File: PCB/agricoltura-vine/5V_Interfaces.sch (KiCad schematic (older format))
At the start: 9 parts, among them K1 G5LE-14_DC5, K2 G5LE-14_DC5, T19 TSW-108-07-G-T, T22 0395121006, U8 TCA6416ARTWR

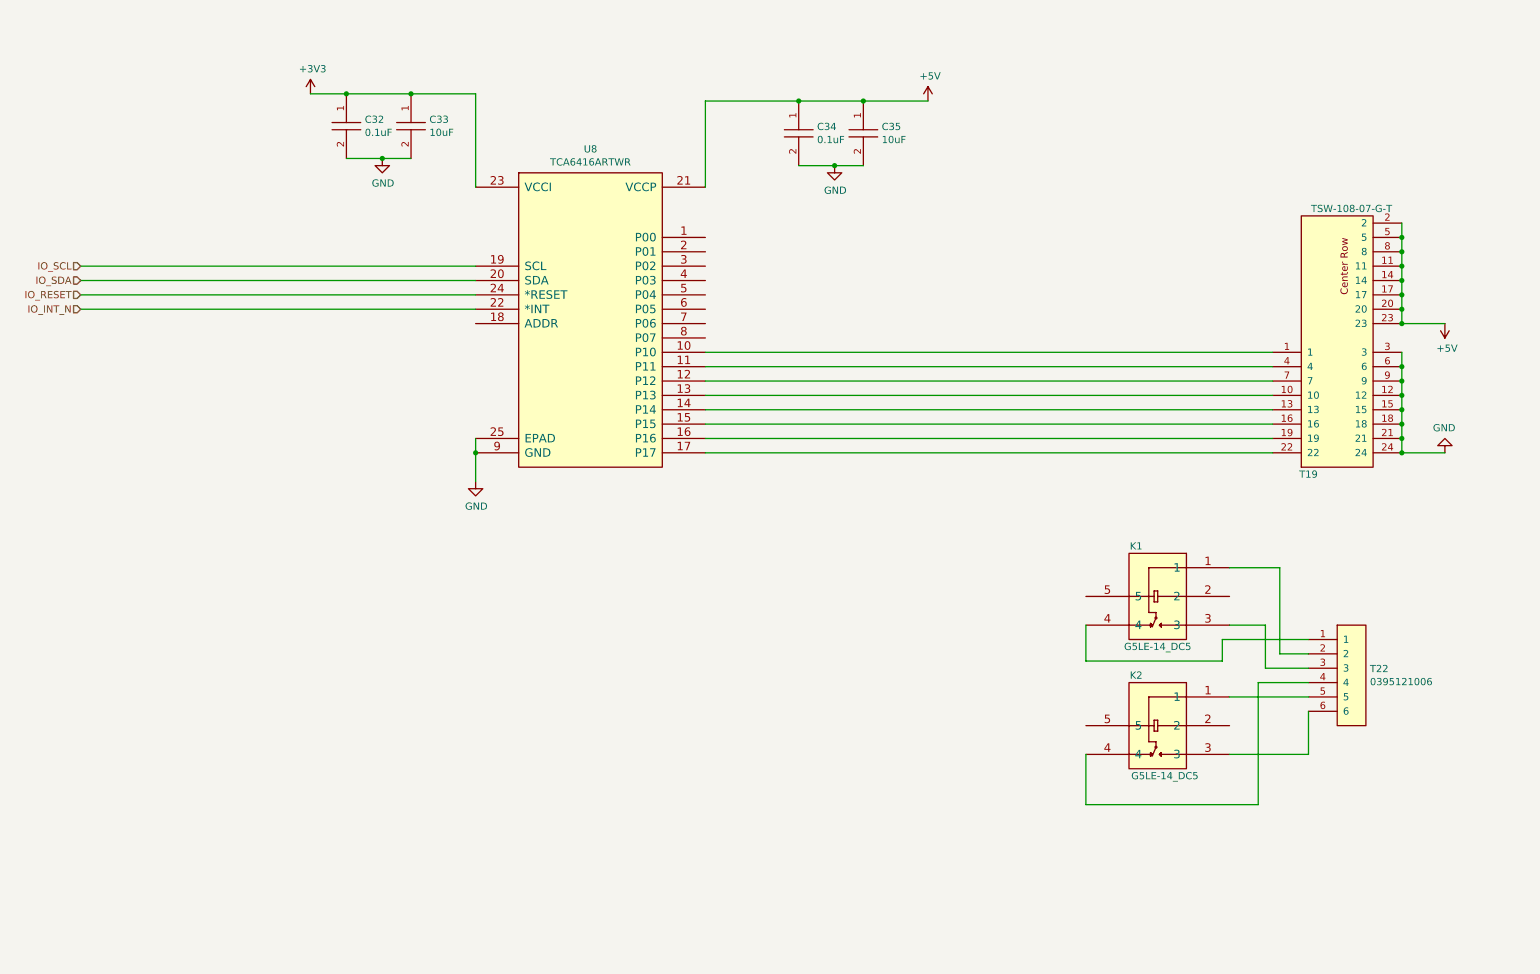
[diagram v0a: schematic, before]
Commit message: Relay Driver Circuit, Board Size Change
Added the Relay driver circuitry, increased size of board tobetter acccomodate relays, figuredout the powerplane topology to get 5Vs where it needs to go.
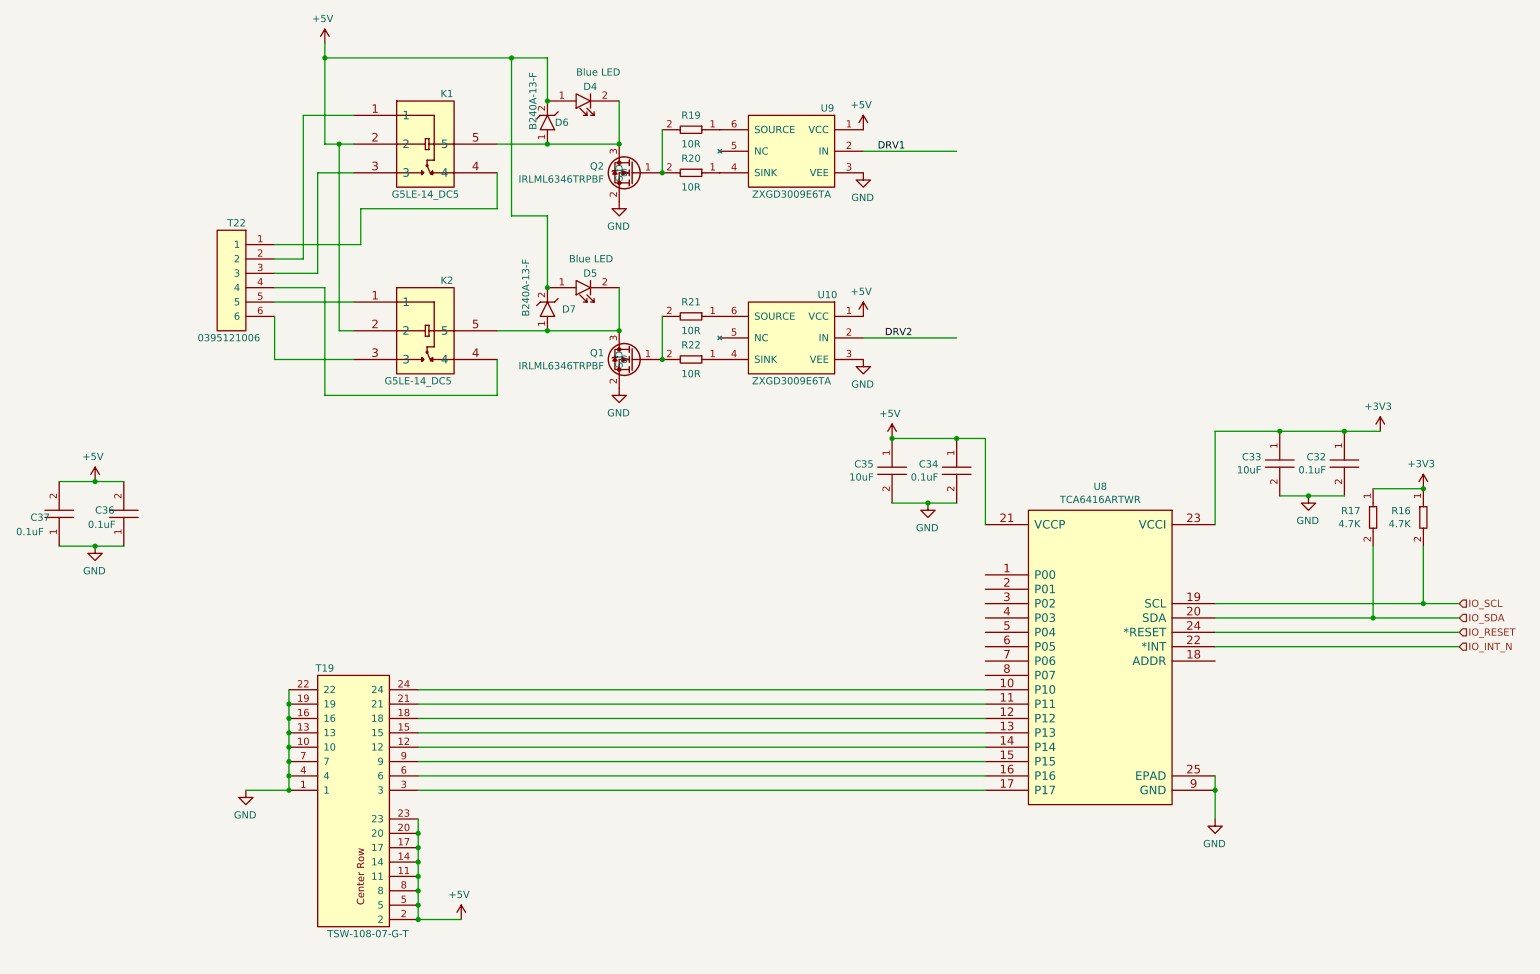
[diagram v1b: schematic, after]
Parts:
- added C36, C37: C0402C104K9PACTU, AVR-KiCAD-Lib-Resistors:R0402, symbol AVR-KiCAD-Lib-Capacitors:C0402C104K9PACTU
- added D4, D5: LTST-C194TBKT, AVR-KiCAD-Lib-Diodes:LED0603, symbol AVR-KiCAD-Lib-Diodes:LTST-C194TBKT
- added D6, D7: B240A-13-F, AVR-KiCAD-Lib-Diodes:B240A-13-F, symbol AVR-KiCAD-Lib-Diodes:B240A-13-F
- added Q1, Q2: IRLML6346TRPBF, AVR-KiCAD-Lib-Transistors:SOT-23, symbol AVR-KiCAD-Lib-Transistors:IRLML6346TRPBF
- added R16, R17: RC0402FR-074K7L, AVR-KiCAD-Lib-Resistors:R0402, symbol AVR-KiCAD-Lib-Resistors:RC0402FR-074K7L
- added R19, R20, R21, R22: RC0402FR-0710RL, AVR-KiCAD-Lib-Resistors:R0402, symbol AVR-KiCAD-Lib-Diodes:RC0402FR-0710RL
- added U10, U9: ZXGD3009E6TA, growbox-KiCAD-ICs:SOT-23-6_Handsoldering, symbol AVR-KiCAD-Lib-ICs:ZXGD3009E6TA
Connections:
- net +3V3: now also R16.1, R17.1
- net +5V: now also K1.2, K2.2, C36.2, C37.2, D4.1, D5.1, D6.2, D7.2, U10.1 (VCC), U9.1 (VCC)
- net GND: now also T19.1, T19.10, T19.13, T19.16, T19.19, T19.22, T19.4, T19.7, C36.1, C37.1, Q1.2 (S), Q2.2 (S), U10.3 (VEE), U9.3 (VEE); no longer T19.12, T19.15, T19.18, T19.21, T19.24, T19.3, T19.6, T19.9
- net IO_SCL: now also R16.2
- net IO_SDA: now also R17.2
- net at K1.5: now also D4.2, D6.1, Q2.3 (D)
- net at K2.5: now also D5.2, D7.1, Q1.3 (D)
- net at U8.10 (P10): now also T19.24; no longer T19.1
- net at U8.11 (P11): now also T19.21; no longer T19.4
- net at U8.12 (P12): now also T19.18; no longer T19.7
- net at U8.13 (P13): now also T19.15; no longer T19.10
- net at U8.14 (P14): now also T19.12; no longer T19.13
- net at U8.15 (P15): now also T19.9; no longer T19.16
- net at U8.16 (P16): now also T19.6; no longer T19.19
- net at U8.17 (P17): now also T19.3; no longer T19.22
- new net: R20.1, U9.4 (SINK)
- new net: R19.1, U9.6 (SOURCE)
- new net: R22.1, U10.4 (SINK)
- new net: R21.1, U10.6 (SOURCE)
- new net: Q2.1 (G), R19.2, R20.2
- new net: Q1.1 (G), R21.2, R22.2
- new net DRV1: U9.2 (IN)
- new net DRV2: U10.2 (IN)
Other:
- moved on the sheet: C32, C33, C34, C35, K1, K2, T19, T22, U8

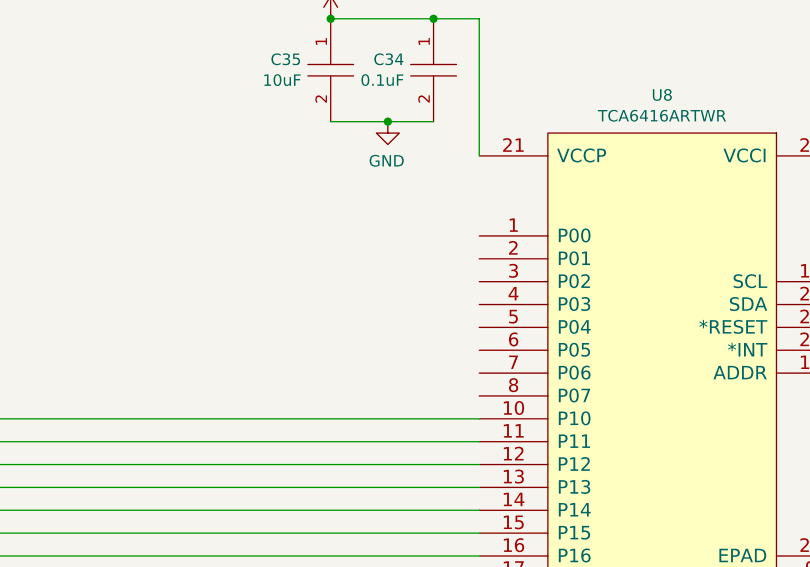
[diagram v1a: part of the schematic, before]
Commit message: First pass of board
Finished routing first pass of PCB
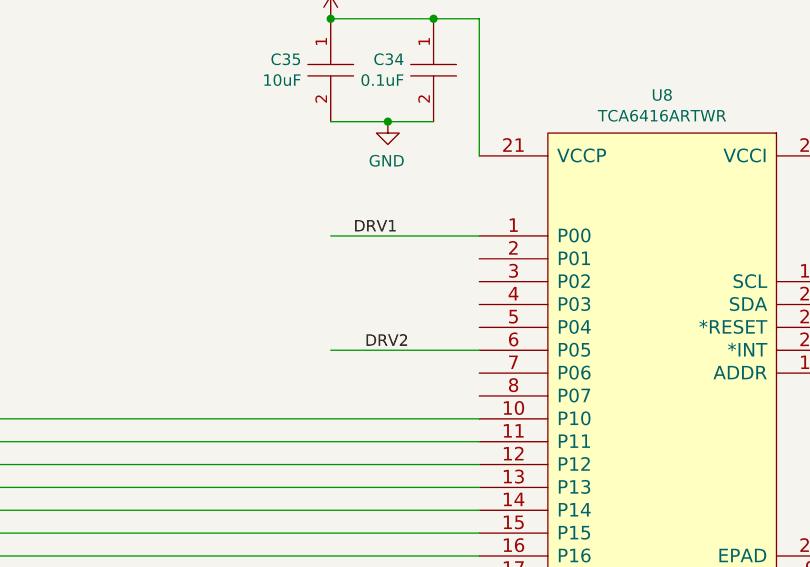
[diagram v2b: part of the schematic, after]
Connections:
- wire segments 89 -> 91
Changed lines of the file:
@@
 Text Label 6750 2850 0    50   ~ 0
 DRV2
+Wire Wire Line
+	6800 4500 7450 4500
+Wire Wire Line
+	6800 5000 7450 5000
+Text Label 6900 4500 0    50   ~ 0
+DRV1
+Text Label 6950 5000 0    50   ~ 0
+DRV2
 $EndSCHEMATC

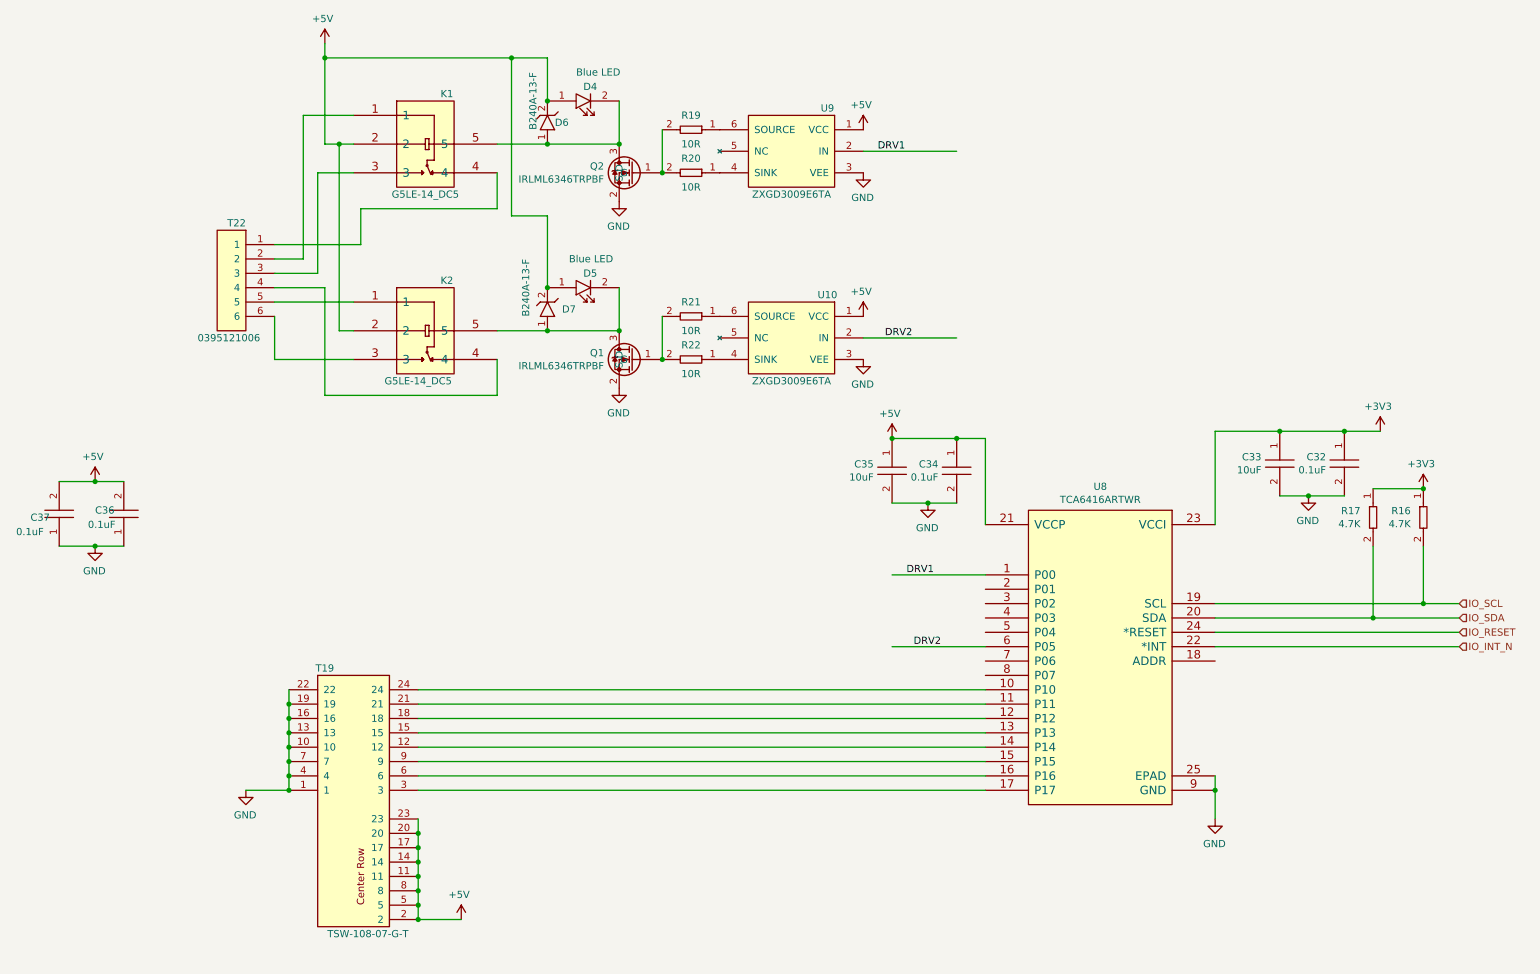
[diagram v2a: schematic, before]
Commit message: Adjustments
Moved Relays closer to edge, pushed VBAT battery holder back towards USB, optimized USB TVS circuit. Broke out extra 5V GPIOs to header
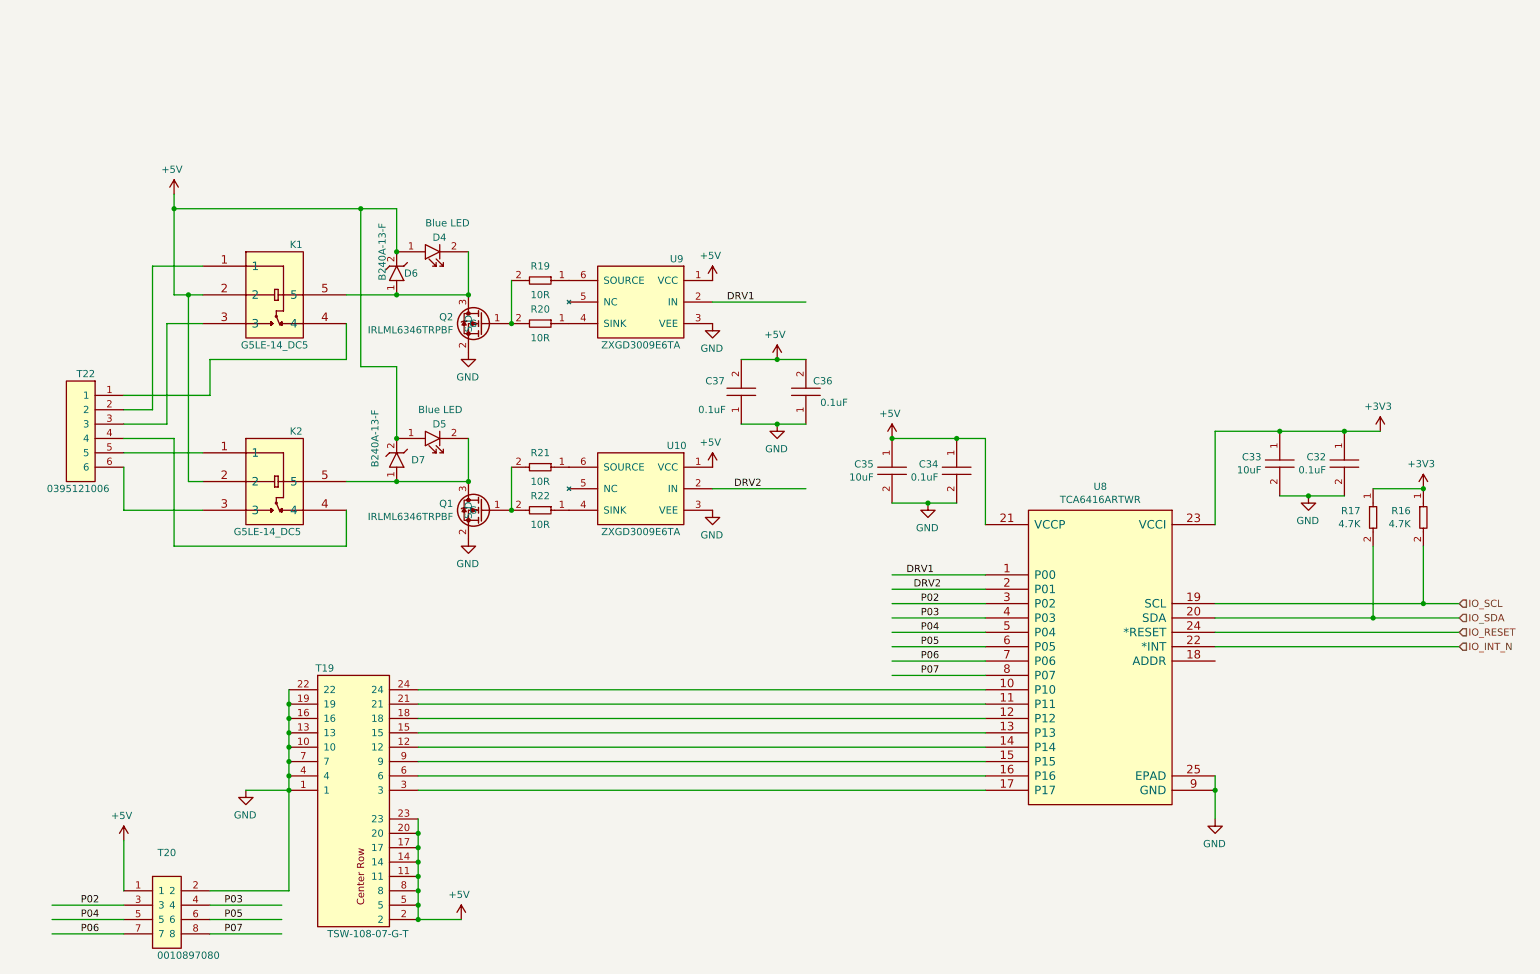
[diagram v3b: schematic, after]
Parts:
- added T20: 0010897080, AVR-KiCAD-Lib-Connectors:Pin_Header_Straight_2x04_Pitch2.54mm, symbol AVR-KiCAD-Lib-Connectors:0010897080
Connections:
- net labels added: P02, P03, P04, P05, P06, P07
- wire segments 91 -> 106
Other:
- moved on the sheet: C36, C37, D4, D5, D6, D7, K1, K2, Q1, Q2, R19, R20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
